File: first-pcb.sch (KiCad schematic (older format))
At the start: 91 parts, among them J1 OLED, SW1 SW_Push, U1 kbd_ProMicro

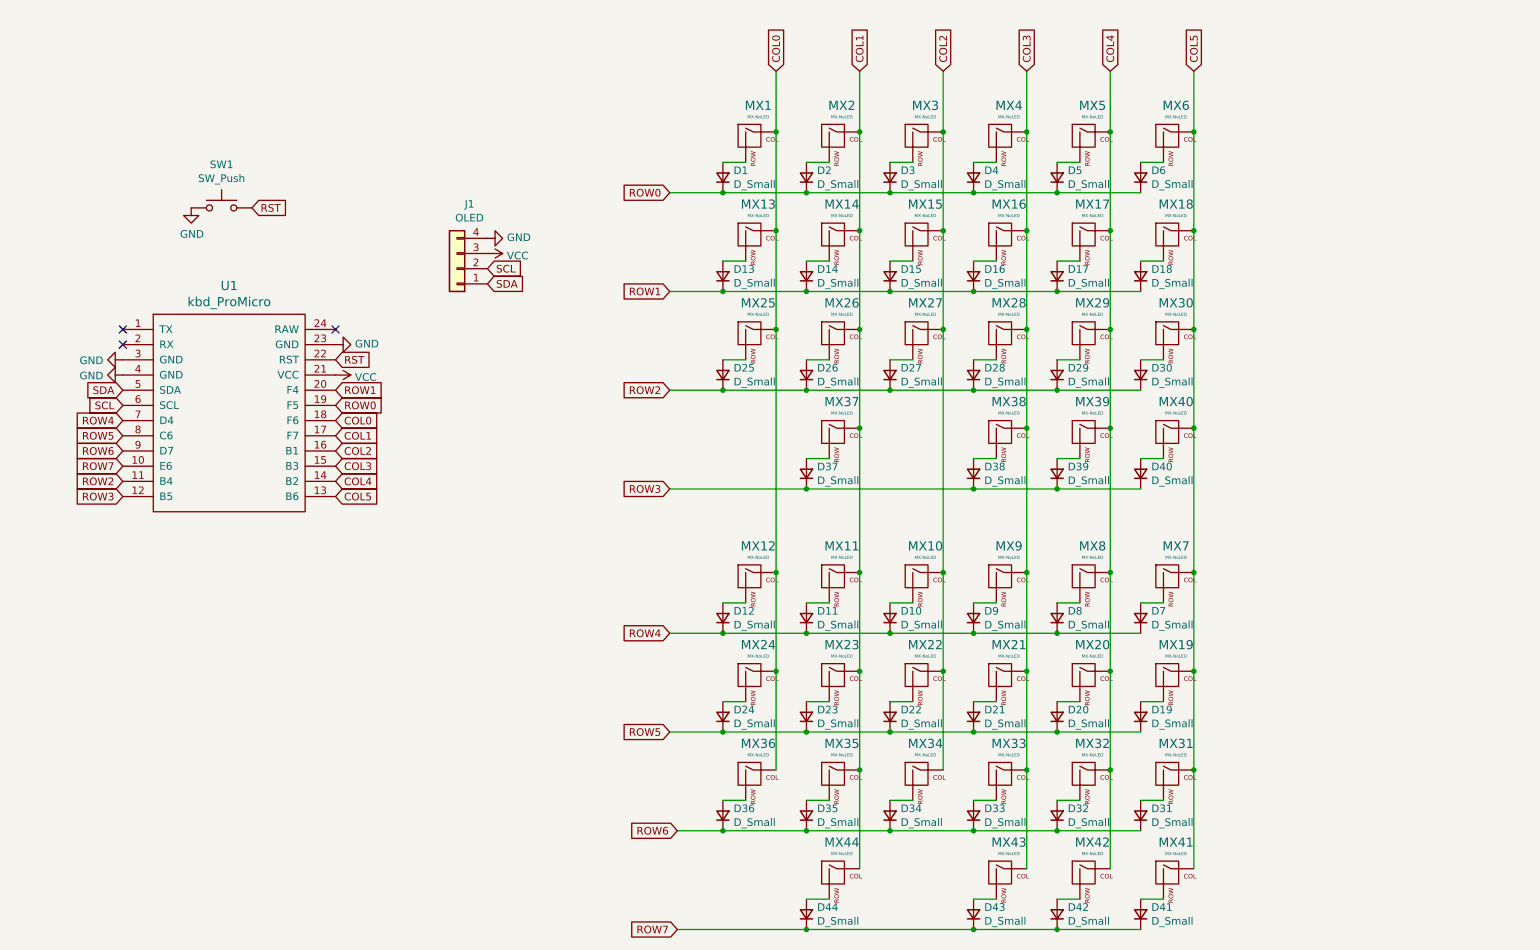
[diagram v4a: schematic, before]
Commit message: Add LED on the schema
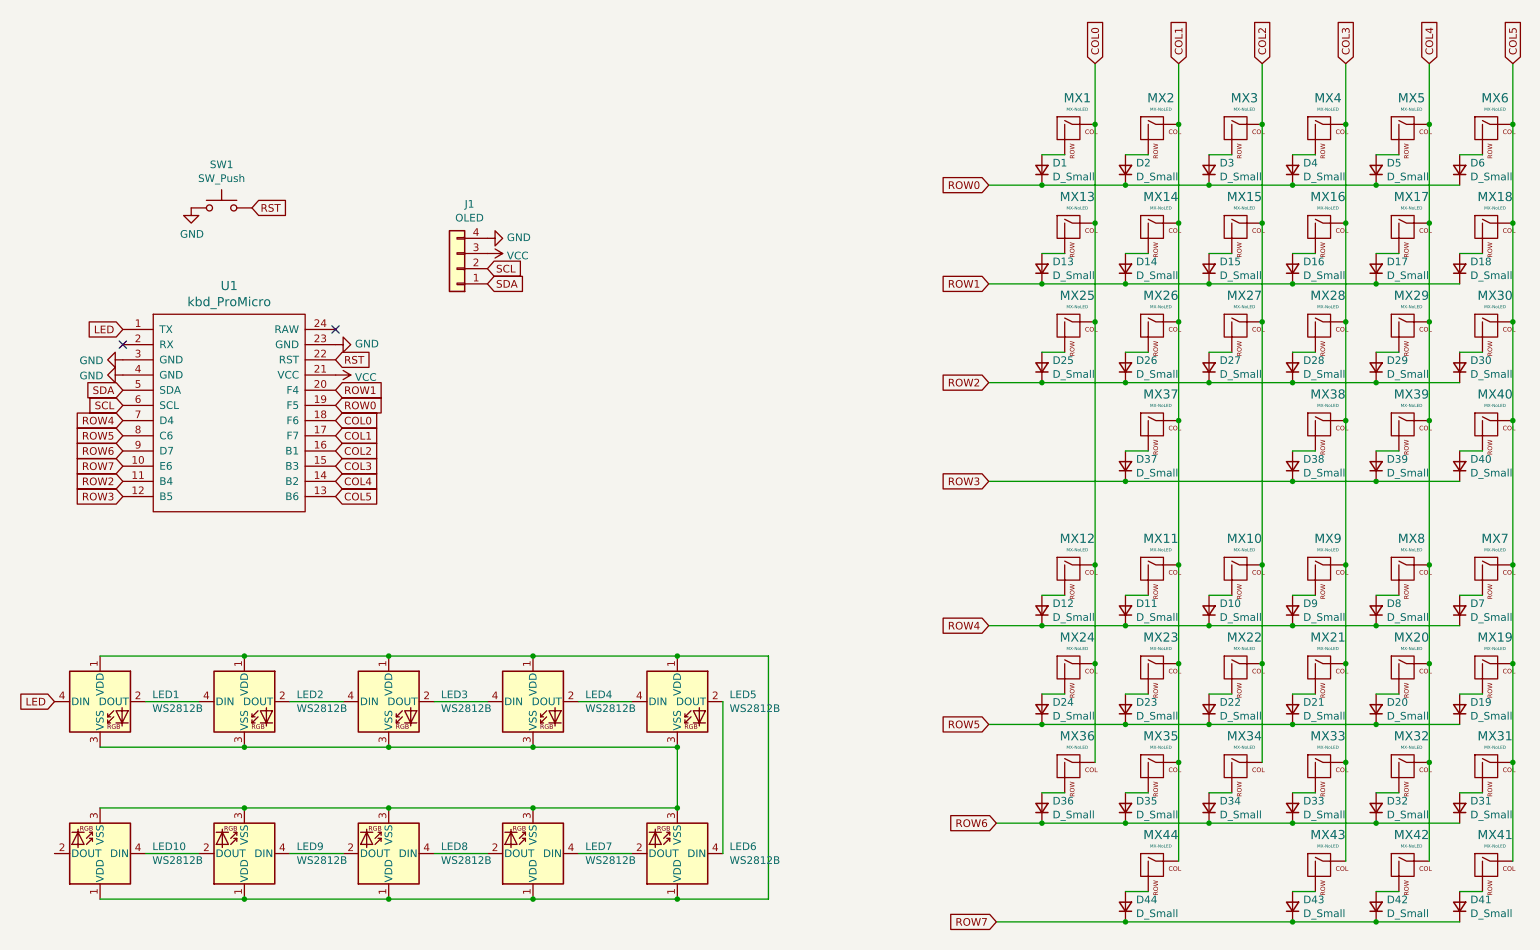
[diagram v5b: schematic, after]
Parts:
- added LED1, LED10, LED2, LED3, LED4, LED5, LED6, LED7, LED8, LED9: WS2812B, LED_SMD:LED_WS2812B_PLCC4_5.0x5.0mm_P3.2mm, symbol LED:WS2812B
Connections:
- net LED: now reaches U1.1 (TX)
- net LED: now also LED1.4 (DIN)
- new net: LED1.1 (VDD), LED10.1 (VDD), LED2.1 (VDD), LED3.1 (VDD), LED4.1 (VDD), LED5.1 (VDD), LED6.1 (VDD), LED7.1 (VDD), LED8.1 (VDD), LED9.1 (VDD)
- new net: LED1.2 (DOUT), LED2.4 (DIN)
- new net: LED1.3 (VSS), LED10.3 (VSS), LED2.3 (VSS), LED3.3 (VSS), LED4.3 (VSS), LED5.3 (VSS), LED6.3 (VSS), LED7.3 (VSS), LED8.3 (VSS), LED9.3 (VSS)
- new net: LED2.2 (DOUT), LED3.4 (DIN)
- new net: LED3.2 (DOUT), LED4.4 (DIN)
- new net: LED4.2 (DOUT), LED5.4 (DIN)
- new net: LED5.2 (DOUT), LED6.4 (DIN)
- new net: LED10.4 (DIN), LED9.2 (DOUT)
- new net: LED8.2 (DOUT), LED9.4 (DIN)
- new net: LED7.2 (DOUT), LED8.4 (DIN)
- new net: LED6.2 (DOUT), LED7.4 (DIN)
- no-connect marks 3 -> 2
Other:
- moved on the sheet: D1, D10, D11, D12, D13, D14, D15, D16, D17, D18, D19, D2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

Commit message: Routing the LED
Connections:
- net GND: now also LED1.1 (VDD), LED10.1 (VDD), LED2.1 (VDD), LED3.1 (VDD), LED4.1 (VDD), LED5.1 (VDD), LED6.1 (VDD), LED7.1 (VDD), LED8.1 (VDD), LED9.1 (VDD)
- net VCC: now also LED1.3 (VSS), LED10.3 (VSS), LED2.3 (VSS), LED3.3 (VSS), LED4.3 (VSS), LED5.3 (VSS), LED6.3 (VSS), LED7.3 (VSS), LED8.3 (VSS), LED9.3 (VSS)
- no-connect marks 2 -> 3
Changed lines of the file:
@@
 	-1   0    0    1
 $EndComp
+$Comp
+L power:GND #PWR0107
+U 1 1 5EAF3A6B
+P 1300 4650
+F 0 "#PWR0107" H 1300 4400 50  0001 C CNN
+F 1 "GND" H 1305 4477 50  0000 C CNN
+F 2 "" H 1300 4650 50  0001 C CNN
+F 3 "" H 1300 4650 50  0001 C CNN
+	1    1300 4650
+	-1   0    0    1
+$EndComp
+Connection ~ 1300 4650
+$Comp
+L power:VCC #PWR0108
+U 1 1 5EAF44CC
+P 1300 5250
+F 0 "#PWR0108" H 1300 5100 50  0001 C CNN
+F 1 "VCC" H 1315 5423 50  0000 C CNN
+F 2 "" H 1300 5250 50  0001 C CNN
+F 3 "" H 1300 5250 50  0001 C CNN
+	1    1300 5250
+	-1   0    0    1
+$EndComp
+Connection ~ 1300 5250
+NoConn ~ 1000 5950
 $EndSCHEMATC

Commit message: Replace smd diode with hybrid
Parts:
- D1, D10, D11, D12, D13, D14, D15, D16, D17, D18, D19, D2, D20, D21, D22, D23, D24, D25, D26, D27, D28, D29, D3, D30, D31, D32, D33, D34, D35, D36, D37, D38, D39, D4, D40, D41, D42, D43, D44, D5, D6, D7, D8, D9: footprint Diode_SMD:D_SOD-123 -> Keebio-Parts:Diode-Hybrid-Back
